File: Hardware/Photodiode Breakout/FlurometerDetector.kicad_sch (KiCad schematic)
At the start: 5 parts, among them U1 OPA336

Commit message: Footprint Assignment
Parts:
- added C2: 10 uF, Capacitor_SMD:C_0603_1608Metric_Pad1.08x0.95mm_HandSolder, symbol Device:C
- C1: value 33.3 uF -> 22 uF; footprint (none) -> Capacitor_SMD:C_0603_1608Metric_Pad1.08x0.95mm_HandSolder
- Conn1: footprint (none) -> MRDT_Connectors:MOLEX_SL_03_Horizontal
- D1: footprint (none) -> Package_TO_SOT_THT:TO-18-2
- R1: value 300 -> 330; footprint (none) -> Resistor_SMD:R_0603_1608Metric_Pad0.98x0.95mm_HandSolder
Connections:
- net +5V: now also C2.1
- net at C1.2, Conn1.3, R1.2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: now also C2.2
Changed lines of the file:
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@@
   (junction (at 203.2 89.535) (diameter 0) (color 0 0 0 0)
   )
+  (junction (at 183.515 80.01) (diameter 0) (color 0 0 0 0)
+  )
   (junction (at 203.2 86.36) (diameter 0) (color 0 0 0 0)
   )
+  (junction (at 169.545 80.01) (diameter 0) (color 0 0 0 0)
+  )
+  (wire (pts (xy 183.515 69.215) (xy 183.515 80.01))
+    (stroke (width 0) (type default) (color 0 0 0 0))
+  )
   (wire (pts (xy 109.22 80.01) (xy 128.27 80.01))
     (stroke (width 0) (type default) (color 0 0 0 0))
@@
     (stroke (width 0) (type default) (color 0 0 0 0))
   )
+  (wire (pts (xy 180.34 69.215) (xy 183.515 69.215))
+    (stroke (width 0) (type default) (color 0 0 0 0))
+  )
   (wire (pts (xy 128.27 90.17) (xy 128.27 86.36))
     (stroke (width 0) (type default) (color 0 0 0 0))
   )
+  (wire (pts (xy 169.545 69.215) (xy 169.545 80.01))
+    (stroke (width 0) (type default) (color 0 0 0 0))
+  )
   (wire (pts (xy 137.16 80.01) (xy 137.16 85.09))
     (stroke (width 0) (type default) (color 0 0 0 0))
   )
+  (wire (pts (xy 169.545 80.01) (xy 172.72 80.01))
+    (stroke (width 0) (type default) (color 0 0 0 0))
+  )
   (wire (pts (xy 152.4 78.74) (xy 152.4 80.01))
     (stroke (width 0) (type default) (color 0 0 0 0))
@@
     (stroke (width 0) (type default) (color 0 0 0 0))
   )
+  (wire (pts (xy 183.515 80.01) (xy 203.2 80.01))
+    (stroke (width 0) (type default) (color 0 0 0 0))
+  )
   (wire (pts (xy 203.2 89.535) (xy 216.535 89.535))
     (stroke (width 0) (type default) (color 0 0 0 0))
   )
-  (wire (pts (xy 152.4 80.01) (xy 172.72 80.01))
+  (wire (pts (xy 152.4 80.01) (xy 169.545 80.01))
+    (stroke (width 0) (type default) (color 0 0 0 0))
+  )
+  (wire (pts (xy 172.72 69.215) (xy 169.545 69.215))
     (stroke (width 0) (type default) (color 0 0 0 0))
   )
@@
     (stroke (width 0) (type default) (color 0 0 0 0))
   )
-  (wire (pts (xy 180.34 80.01) (xy 203.2 80.01))
+  (wire (pts (xy 180.34 80.01) (xy 183.515 80.01))
     (stroke (width 0) (type default) (color 0 0 0 0))
   )
@@
       (effects (font (size 1.524 1.524)) (justify left))
     )
-    (property "Footprint" "" (id 2) (at 221.615 90.805 0)
+    (property "Footprint" "MRDT_Connectors:MOLEX_SL_03_Horizontal" (id 2) (at 221.615 90.805 0)
       (effects (font (size 1.524 1.524)) hide)
     )
@@
       (effects (font (size 1.27 1.27)) (justify left))
     )
-    (property "Footprint" "" (id 2) (at 109.22 87.63 0)
+    (property "Footprint" "Package_TO_SOT_THT:TO-18-2" (id 2) (at 109.22 87.63 0)
       (effects (font (size 1.27 1.27)) hide)
     )
@@
     (in_bom yes) (on_board yes)
     (property "Reference" "R1" (id 0) (at 176.53 83.82 90))
-    (property "Value" "300" (id 1) (at 176.53 86.36 90))
-    (property "Footprint" "" (id 2) (at 176.53 88.138 90)
+    (property "Value" "330" (id 1) (at 176.53 86.36 90))
+    (property "Footprint" "Resistor_SMD:R_0603_1608Metric_Pad0.98x0.95mm_HandSolder" (id 2) (at 176.53 88.138 90)
       (effects (font (size 1.27 1.27)) hide)
     )
@@
     (in_bom yes) (on_board yes) (fields_autoplaced)
     (property "Reference" "C1" (id 0) (at 176.53 74.1512 90))
-    (property "Value" "33.3 uF" (id 1) (at 176.53 76.6881 90))
-    (property "Footprint" "" (id 2) (at 180.34 79.0448 0)
+    (property "Value" "22 uF" (id 1) (at 176.53 76.6881 90))
+    (property "Footprint" "Capacitor_SMD:C_0603_1608Metric_Pad1.08x0.95mm_HandSolder" (id 2) (at 180.34 79.0448 0)
       (effects (font (size 1.27 1.27)) hide)
     )
     (property "Datasheet" "~" (id 3) (at 176.53 80.01 0)
+      (effects (font (size 1.27 1.27)) hide)
+    )
+    (pin "1")
+    (pin "2")
+  )
+  (symbol (lib_id "Device:C") (at 176.53 69.215 90) (unit 1)
+    (in_bom yes) (on_board yes) (fields_autoplaced)
+    (property "Reference" "C2" (id 0) (at 176.53 63.3562 90))
+    (property "Value" "10 uF" (id 1) (at 176.53 65.8931 90))
+    (property "Footprint" "Capacitor_SMD:C_0603_1608Metric_Pad1.08x0.95mm_HandSolder" (id 2) (at 180.34 68.2498 0)
+      (effects (font (size 1.27 1.27)) hide)
+    )
+    (property "Datasheet" "~" (id 3) (at 176.53 69.215 0)
       (effects (font (size 1.27 1.27)) hide)
     )
@@
     )
     (path "/bccfd91a-8dd7-4ef2-b894-a13e7be2688e"
-      (reference "C1") (unit 1) (value "33.3 uF") (footprint "")
+      (reference "C1") (unit 1) (value "22 uF") (footprint "Capacitor_SMD:C_0603_1608Metric_Pad1.08x0.95mm_HandSolder")
+    )
+    (path "/d7670f7e-1f5f-4edb-82aa-698a714b8a53"
+      (reference "C2") (unit 1) (value "10 uF") (footprint "Capacitor_SMD:C_0603_1608Metric_Pad1.08x0.95mm_HandSolder")
     )
     (path "/21803a30-7ef9-4631-9b8c-b17a9b1f579b"
-      (reference "Conn1") (unit 1) (value "Molex_SL_03") (footprint "")
+      (reference "Conn1") (unit 1) (value "Molex_SL_03") (footprint "MRDT_Connectors:MOLEX_SL_03_Horizontal")
     )
     (path "/3a965256-e763-47ad-a606-4ab4b3f141f0"
-      (reference "D1") (unit 1) (value "D_Photo") (footprint "")
+      (reference "D1") (unit 1) (value "D_Photo") (footprint "Package_TO_SOT_THT:TO-18-2")
     )
     (path "/71395b4f-bbbe-4b5b-9921-09233906f6de"
-      (reference "R1") (unit 1) (value "300") (footprint "")
+      (reference "R1") (unit 1) (value "330") (footprint "Resistor_SMD:R_0603_1608Metric_Pad0.98x0.95mm_HandSolder")
     )
     (path "/f7ce3aef-c83c-4988-90fe-5a1f92cb211f"

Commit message: Added 2nd Photodiode, Fixed OpAmp
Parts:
- removed Conn1: Molex_SL_03, MRDT_Connectors:MOLEX_SL_03_Horizontal, symbol MRDT_Connectors:Molex_SL_03
- added C3: 10 uF, Capacitor_SMD:C_0603_1608Metric_Pad1.08x0.95mm_HandSolder, symbol Device:C
- added C4: 22 uF, Capacitor_SMD:C_0603_1608Metric_Pad1.08x0.95mm_HandSolder, symbol Device:C
- added Conn1: Molex_SL_04, MRDT_Connectors:MOLEX_SL_04_Vertical, symbol MRDT_Connectors:Molex_SL_04
- added D2: D_Photo, Package_TO_SOT_THT:TO-18-2, symbol Device:D_Photo
- added R2: 330, Resistor_SMD:R_0603_1608Metric_Pad0.98x0.95mm_HandSolder, symbol Device:R
- added U2: OPA336, Package_SO:SOIC-8_3.9x4.9mm_P1.27mm, symbol Amplifier_Operational:OPA333xxD
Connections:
- net +5V: now also Conn1.1, U2.7 (V+); no longer C1.1, C2.1, D1.1 (K), R1.1, U1.3 (+)
- net GND: now also U1.3 (+), Conn1.2, D2.2 (A), U2.3 (+), U2.4 (V-); no longer U1.2 (-)
- net at C1.2, C2.2, R1.2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: now also Conn1.3
- new net: C3.1, C4.1, D2.1 (K), R2.1, U2.2 (-)
- new net: C3.2, C4.2, Conn1.4, R2.2, U2.6
- new net: C1.1, C2.1, D1.1 (K), R1.1, U1.2 (-)
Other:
- moved on the sheet: D1

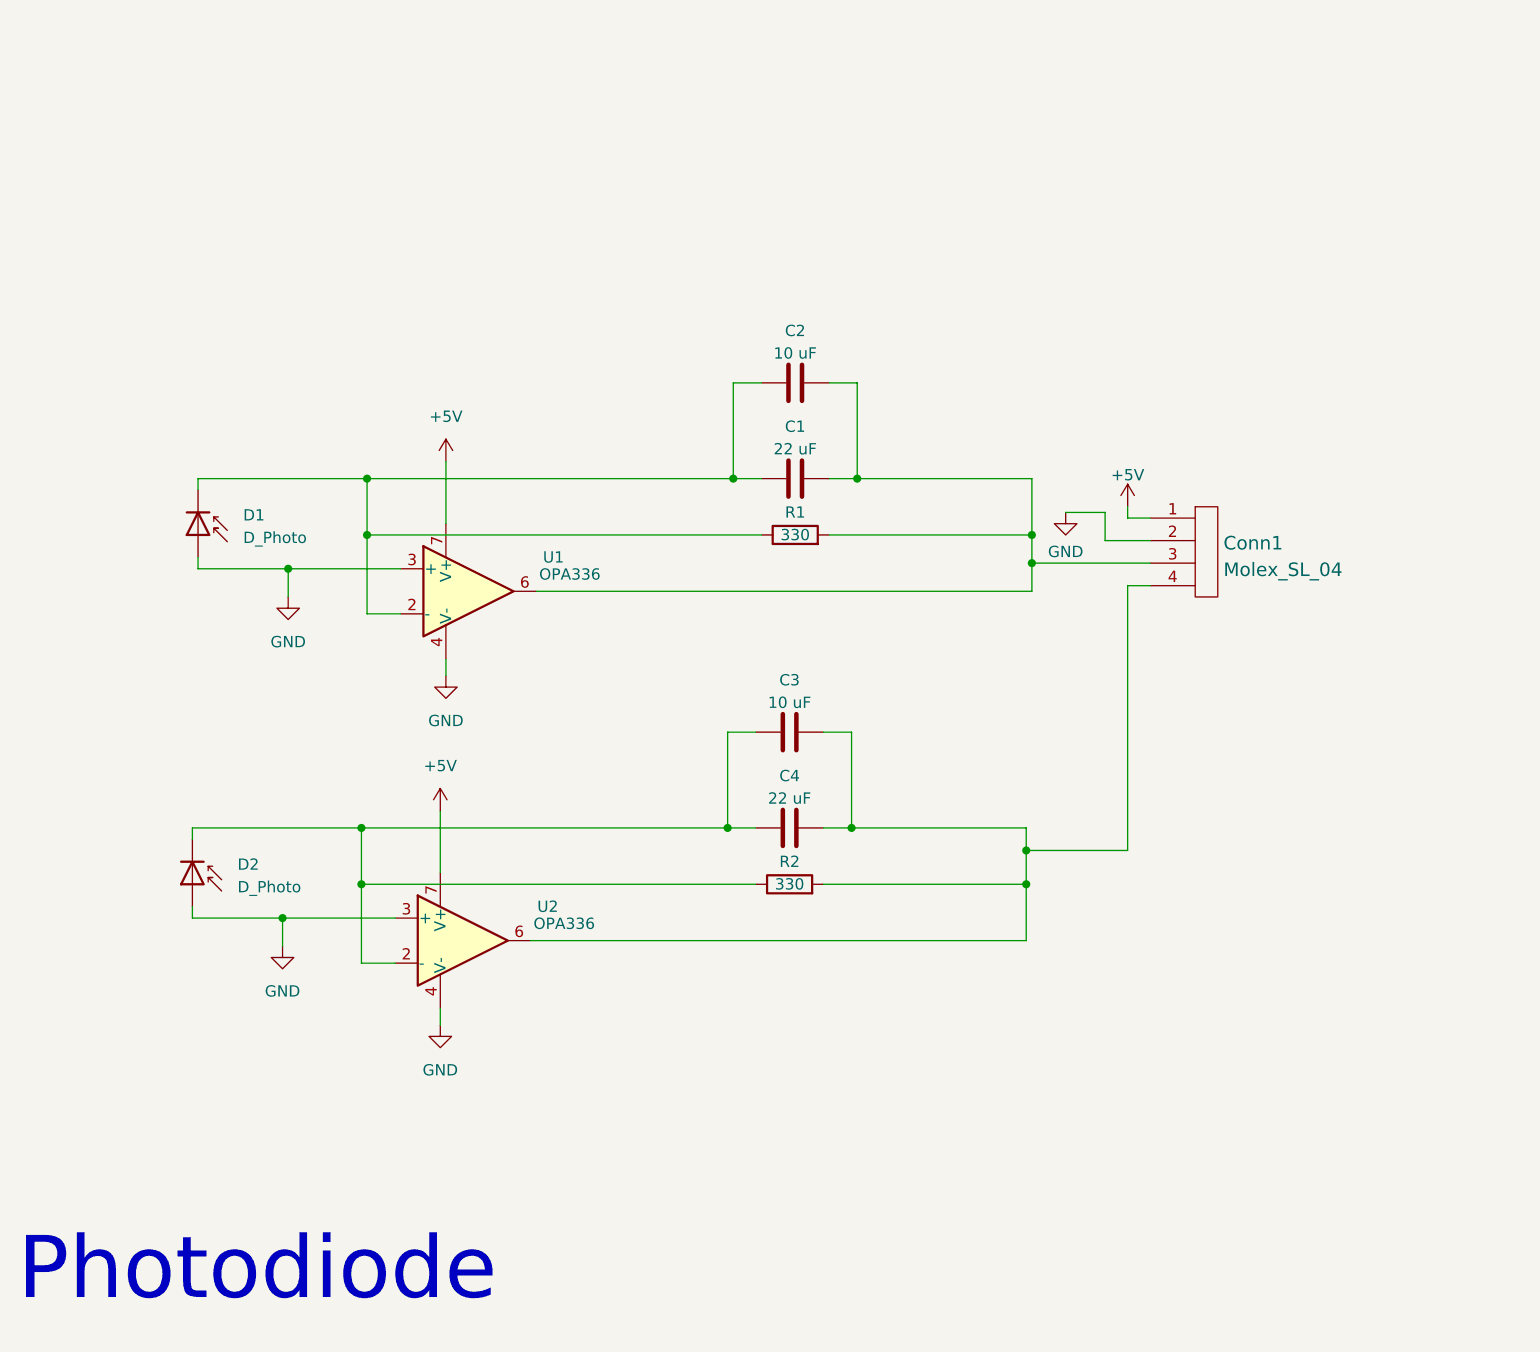
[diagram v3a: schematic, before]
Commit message: Mosfets & H-Bridge Organized, Photodiode organized, Footprints for LED
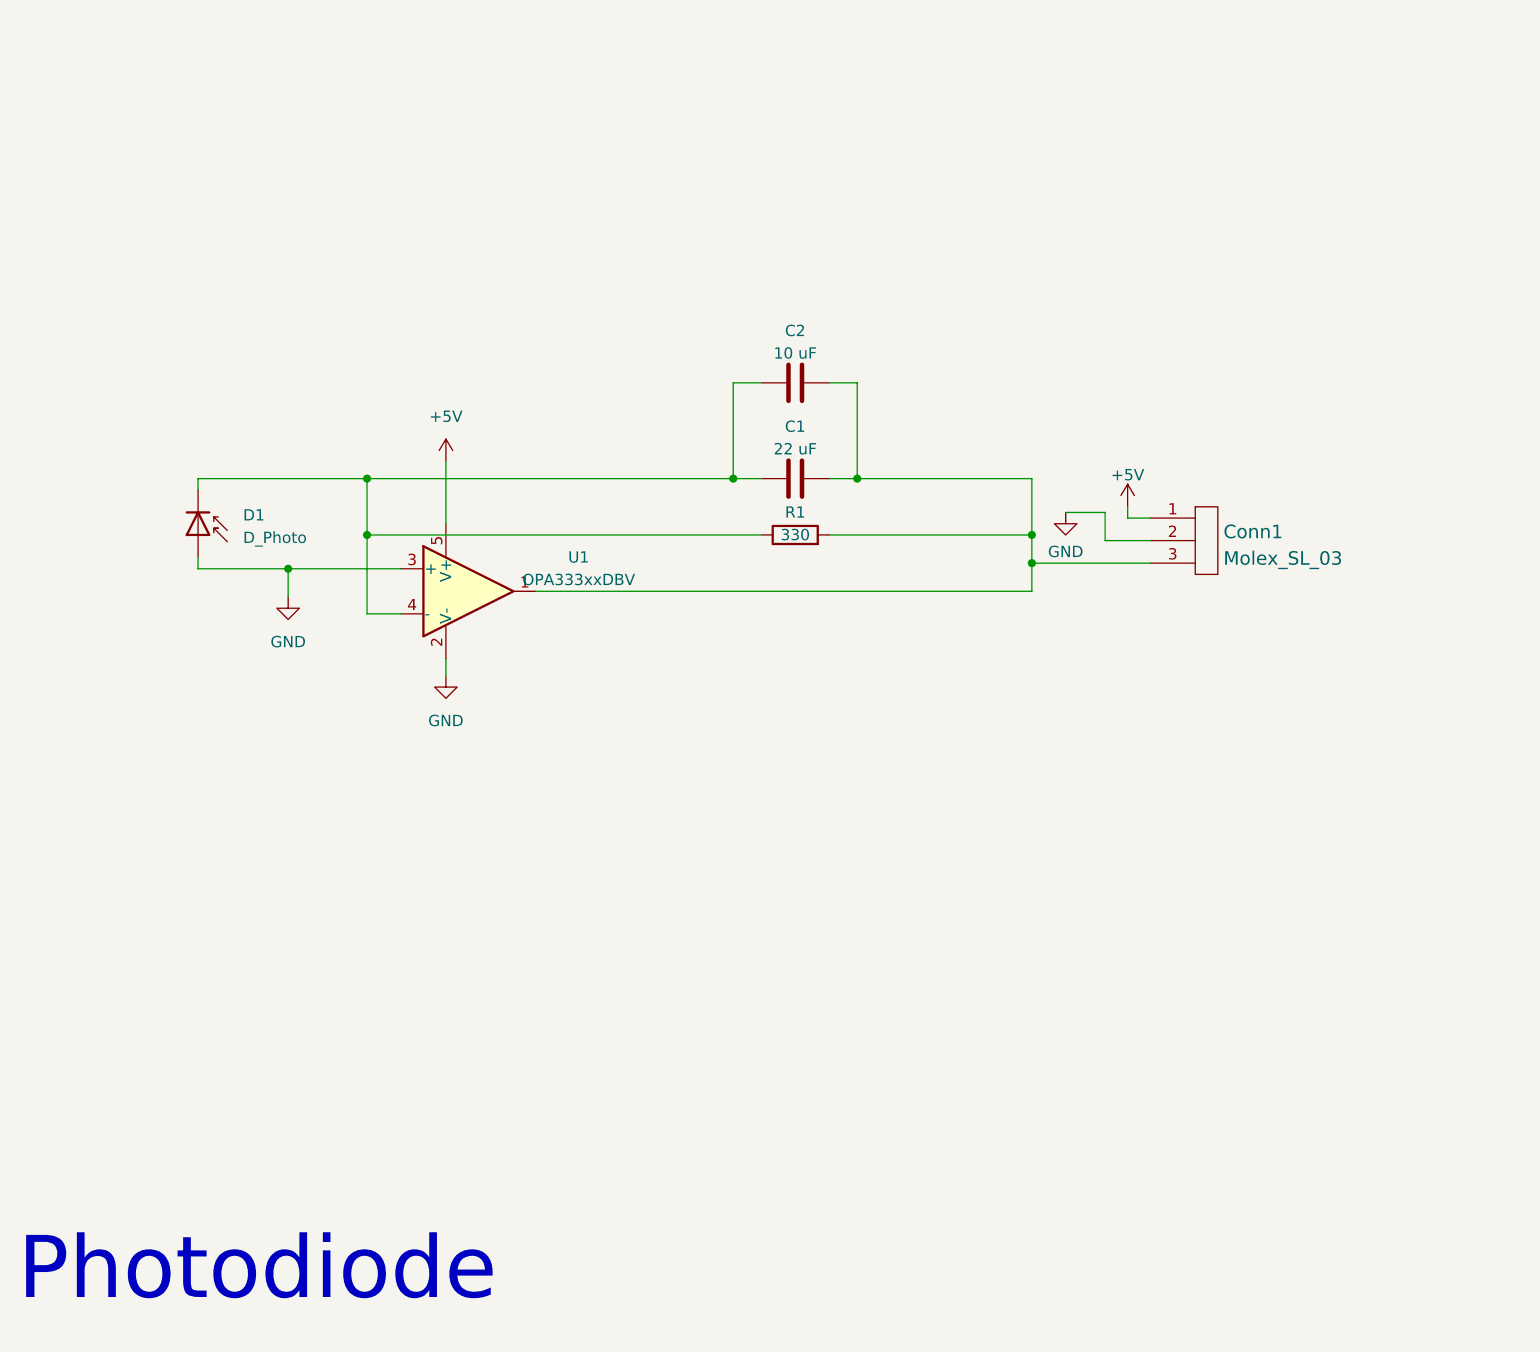
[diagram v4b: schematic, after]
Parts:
- removed C3: 10 uF, Capacitor_SMD:C_0603_1608Metric_Pad1.08x0.95mm_HandSolder, symbol Device:C
- removed C4: 22 uF, Capacitor_SMD:C_0603_1608Metric_Pad1.08x0.95mm_HandSolder, symbol Device:C
- removed Conn1: Molex_SL_04, MRDT_Connectors:MOLEX_SL_04_Vertical, symbol MRDT_Connectors:Molex_SL_04
- removed D2: D_Photo, Package_TO_SOT_THT:TO-18-2, symbol Device:D_Photo
- removed R2: 330, Resistor_SMD:R_0603_1608Metric_Pad0.98x0.95mm_HandSolder, symbol Device:R
- removed U1, U2: OPA336, Package_SO:SOIC-8_3.9x4.9mm_P1.27mm, symbol Amplifier_Operational:OPA333xxD
- added Conn1: Molex_SL_03, MRDT_Connectors:MOLEX_SL_03_Horizontal, symbol MRDT_Connectors:Molex_SL_03
- added U1: OPA333xxDBV, Package_TO_SOT_SMD:SOT-23-5, symbol Amplifier_Operational:OPA333xxDBV
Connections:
- net +5V: now also Conn1.1, U1.5 (V+)
- net GND: now also Conn1.2, U1.2 (V-), U1.3 (+)
- net at C1.1, C2.1, D1.1 (K)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: now also U1.4 (-)
- net at C1.2, C2.2, R1.2: now also Conn1.3, U1.1

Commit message: Breakout Boards
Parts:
- added V1, V2, V3, V4: Via, MRDT_Drill_Holes:4_40_Hole, symbol MRDT_Drill_Holes:Via
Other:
- note added: "Vias"
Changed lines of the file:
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@@
     (stroke (width 0) (type default) (color 0 0 0 0))
   )
-  (text "Photodiode" (at 88.9 173.355 0)
+  (text "Vias" (at 236.855 50.165 0)
+    (effects (font (size 4 4)) (justify left bottom))
+  )
+  (text "Photodiode" (at 140.335 122.555 0)
     (effects (font (size 7 7)) (justify left bottom))
+  )
+  (symbol (lib_id "MRDT_Drill_Holes:Via") (at 247.65 31.115 0) (unit 1)
+    (in_bom yes) (on_board yes)
+    (property "Reference" "V3" (id 0) (at 253.4412 29.6418 0)
+      (effects (font (size 1.524 1.524)) (justify left))
+    )
+    (property "Value" "Via" (id 1) (at 253.4412 32.3342 0)
+      (effects (font (size 1.524 1.524)) (justify left))
+    )
+    (property "Footprint" "MRDT_Drill_Holes:4_40_Hole" (id 2) (at 247.65 31.115 0)
+      (effects (font (size 1.524 1.524)) hide)
+    )
+    (property "Datasheet" "" (id 3) (at 247.65 31.115 0)
+      (effects (font (size 1.524 1.524)) hide)
+    )
+    (pin "1")
   )
   (symbol (lib_id "MRDT_Connectors:Molex_SL_03") (at 221.615 90.805 0) (unit 1)
@@
     (property "Datasheet" "" (id 3) (at 137.16 78.105 0)
       (effects (font (size 1.27 1.27)) hide)
+    )
+    (pin "1")
+  )
+  (symbol (lib_id "MRDT_Drill_Holes:Via") (at 230.505 31.115 0) (unit 1)
+    (in_bom yes) (on_board yes)
+    (property "Reference" "V1" (id 0) (at 236.2962 29.6418 0)
+      (effects (font (size 1.524 1.524)) (justify left))
+    )
+    (property "Value" "Via" (id 1) (at 236.2962 32.3342 0)
+      (effects (font (size 1.524 1.524)) (justify left))
+    )
+    (property "Footprint" "MRDT_Drill_Holes:4_40_Hole" (id 2) (at 230.505 31.115 0)
+      (effects (font (size 1.524 1.524)) hide)
+    )
+    (property "Datasheet" "" (id 3) (at 230.505 31.115 0)
+      (effects (font (size 1.524 1.524)) hide)
     )
     (pin "1")
@@
     (pin "1")
   )
+  (symbol (lib_id "MRDT_Drill_Holes:Via") (at 230.505 38.735 0) (unit 1)
+    (in_bom yes) (on_board yes)
+    (property "Reference" "V2" (id 0) (at 236.2962 37.2618 0)
+      (effects (font (size 1.524 1.524)) (justify left))
+    )
+    (property "Value" "Via" (id 1) (at 236.2962 39.9542 0)
+      (effects (font (size 1.524 1.524)) (justify left))
+    )
+    (property "Footprint" "MRDT_Drill_Holes:4_40_Hole" (id 2) (at 230.505 38.735 0)
+      (effects (font (size 1.524 1.524)) hide)
+    )
+    (property "Datasheet" "" (id 3) (at 230.505 38.735 0)
+      (effects (font (size 1.524 1.524)) hide)
+    )
+    (pin "1")
+  )
   (symbol (lib_id "power:+5V") (at 213.995 83.185 0) (unit 1)
     (in_bom yes) (on_board yes) (fields_autoplaced)
@@
     (property "Datasheet" "" (id 3) (at 213.995 83.185 0)
       (effects (font (size 1.27 1.27)) hide)
+    )
+    (pin "1")
+  )
+  (symbol (lib_id "MRDT_Drill_Holes:Via") (at 247.65 38.735 0) (unit 1)
+    (in_bom yes) (on_board yes)
+    (property "Reference" "V4" (id 0) (at 253.4412 37.2618 0)
+      (effects (font (size 1.524 1.524)) (justify left))
+    )
+    (property "Value" "Via" (id 1) (at 253.4412 39.9542 0)
+      (effects (font (size 1.524 1.524)) (justify left))
+    )
+    (property "Footprint" "MRDT_Drill_Holes:4_40_Hole" (id 2) (at 247.65 38.735 0)
+      (effects (font (size 1.524 1.524)) hide)
+    )
+    (property "Datasheet" "" (id 3) (at 247.65 38.735 0)
+      (effects (font (size 1.524 1.524)) hide)
     )
     (pin "1")
@@
       (reference "U1") (unit 1) (value "OPA333xxDBV") (footprint "Package_TO_SOT_SMD:SOT-23-5")
     )
-  )
+    (path "/752d59e6-914b-40e9-8d9d-483e855b8b52"
+      (reference "V1") (unit 1) (value "Via") (footprint "MRDT_Drill_Holes:4_40_Hole")
+    )
+    (path "/ea8469c4-e106-4a6e-a980-53f6c9b5cdb9"
+      (reference "V2") (unit 1) (value "Via") (footprint "MRDT_Drill_Holes:4_40_Hole")
+    )
+    (path "/0f41a2da-fca3-442a-ad32-5d58a0b3b5ca"
+      (reference "V3") (unit 1) (value "Via") (footprint "MRDT_Drill_Holes:4_40_Hole")
+    )
+    (path "/f7cfcd30-d70d-4ffe-bf8e-5b47b83b5891"
+      (reference "V4") (unit 1) (value "Via") (footprint "MRDT_Drill_Holes:4_40_Hole")
+    )
+  )
